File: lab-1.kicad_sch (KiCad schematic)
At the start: 0 parts

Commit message: Added decoupling capacitors
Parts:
- added C0: 4.7u, Capacitor_SMD:C_0201_0603Metric_Pad0.64x0.40mm_HandSolder, symbol Device:C
- added C1, C2, C3, C4, C5: 100n, Capacitor_SMD:C_0201_0603Metric_Pad0.64x0.40mm_HandSolder, symbol Device:C
- added C6: 10n, Capacitor_SMD:C_0201_0603Metric_Pad0.64x0.40mm_HandSolder, symbol Device:C
- added C7, C8: 1u, Capacitor_SMD:C_0201_0603Metric_Pad0.64x0.40mm_HandSolder, symbol Device:C
- added FB1: 120, Inductor_SMD:L_0201_0603Metric_Pad0.64x0.40mm_HandSolder, symbol Device:FerriteBead
- added U1: STM32F405RGTx, Package_QFP:LQFP-64_10x10mm_P0.5mm, symbol MCU_ST_STM32F4:STM32F405RGTx
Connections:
- new net +3.3V: C0.1, C1.1, C2.1, C3.1, C4.1, C5.1, C8.1, FB1.2, U1.1 (VBAT), U1.19 (VDD), U1.32 (VDD), U1.48 (VDD), U1.64 (VDD)
- new net +3.3VA: C6.1, C7.1, FB1.1, U1.13 (VDDA)
- new net GND: C0.2, C1.2, C2.2, C3.2, C4.2, C5.2, C6.2, C7.2, C8.2, U1.12 (VSSA), U1.18 (VSS), U1.63 (VSS)

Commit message: Changed the footprints + track width
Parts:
- C0, C7, C8: footprint Capacitor_SMD:C_0201_0603Metric_Pad0.64x0.40mm_HandSolder -> Capacitor_SMD:C_0603_1608Metric
- C1, C2, C3, C4, C5, C6: footprint Capacitor_SMD:C_0201_0603Metric_Pad0.64x0.40mm_HandSolder -> Capacitor_SMD:C_0402_1005Metric
- FB1: footprint Inductor_SMD:L_0201_0603Metric_Pad0.64x0.40mm_HandSolder -> Inductor_SMD:L_0603_1608Metric
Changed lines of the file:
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@@
 			)
 		)
-		(property "Footprint" "Capacitor_SMD:C_0201_0603Metric_Pad0.64x0.40mm_HandSolder"
+		(property "Footprint" "Capacitor_SMD:C_0402_1005Metric"
 			(at 176.2252 38.1 0)
 			(effects
@@
 			)
 		)
-		(property "Footprint" "Capacitor_SMD:C_0201_0603Metric_Pad0.64x0.40mm_HandSolder"
+		(property "Footprint" "Capacitor_SMD:C_0402_1005Metric"
 			(at 134.3152 38.1 0)
 			(effects
@@
 			)
 		)
-		(property "Footprint" "Capacitor_SMD:C_0201_0603Metric_Pad0.64x0.40mm_HandSolder"
+		(property "Footprint" "Capacitor_SMD:C_0603_1608Metric"
 			(at 210.5152 38.1 0)
 			(effects
@@
 			)
 		)
-		(property "Footprint" "Capacitor_SMD:C_0201_0603Metric_Pad0.64x0.40mm_HandSolder"
+		(property "Footprint" "Capacitor_SMD:C_0402_1005Metric"
 			(at 113.9952 38.1 0)
 			(effects
@@
 			)
 		)
-		(property "Footprint" "Capacitor_SMD:C_0201_0603Metric_Pad0.64x0.40mm_HandSolder"
+		(property "Footprint" "Capacitor_SMD:C_0402_1005Metric"
 			(at 124.1552 38.1 0)
 			(effects
@@
 			)
 		)
-		(property "Footprint" "Capacitor_SMD:C_0201_0603Metric_Pad0.64x0.40mm_HandSolder"
+		(property "Footprint" "Capacitor_SMD:C_0402_1005Metric"
 			(at 93.6752 38.1 0)
 			(effects
@@
 			)
 		)
-		(property "Footprint" "Capacitor_SMD:C_0201_0603Metric_Pad0.64x0.40mm_HandSolder"
+		(property "Footprint" "Capacitor_SMD:C_0402_1005Metric"
 			(at 103.8352 38.1 0)
 			(effects
@@
 			)
 		)
-		(property "Footprint" "Capacitor_SMD:C_0201_0603Metric_Pad0.64x0.40mm_HandSolder"
+		(property "Footprint" "Capacitor_SMD:C_0603_1608Metric"
 			(at 186.3852 38.1 0)
 			(effects
@@
 			)
 		)
-		(property "Footprint" "Inductor_SMD:L_0201_0603Metric_Pad0.64x0.40mm_HandSolder"
+		(property "Footprint" "Inductor_SMD:L_0603_1608Metric"
 			(at 198.12 30.988 90)
 			(effects
@@
 			)
 		)
-		(property "Footprint" "Capacitor_SMD:C_0201_0603Metric_Pad0.64x0.40mm_HandSolder"
+		(property "Footprint" "Capacitor_SMD:C_0603_1608Metric"
 			(at 83.5152 38.1 0)
 			(effects

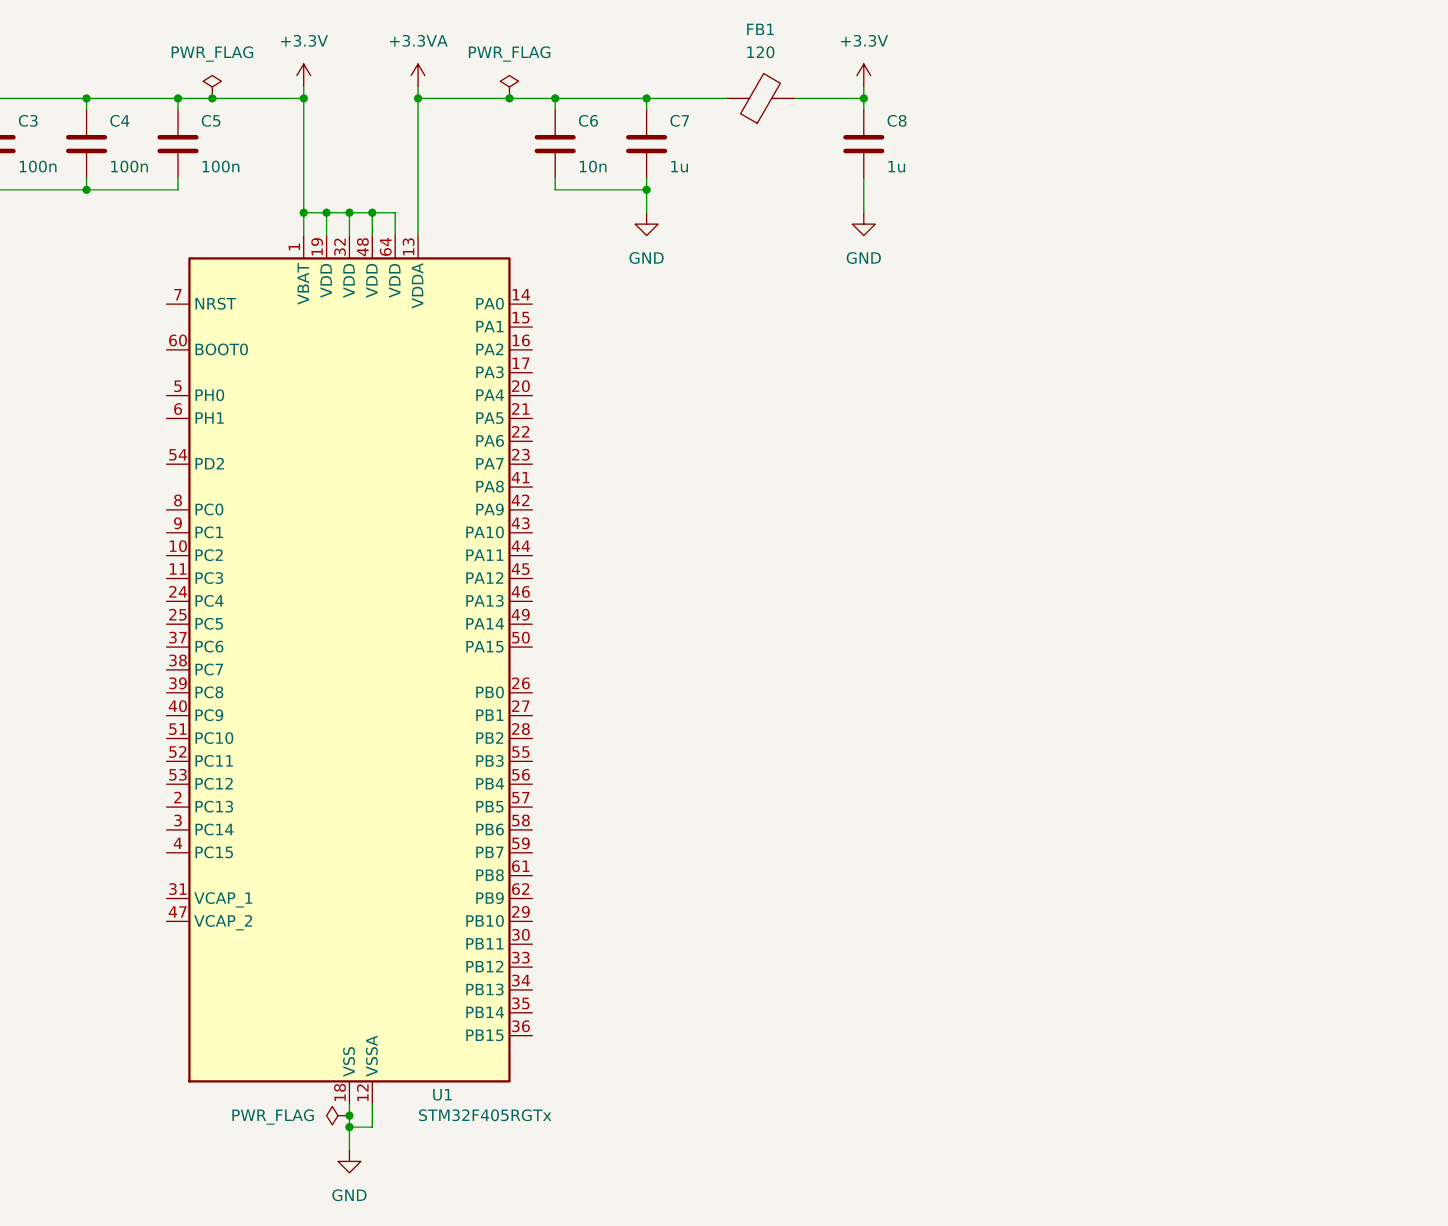
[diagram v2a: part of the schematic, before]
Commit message: Modified tracks and capacitor placing Added type-c and LDO MCP1700 as source of power for STM
Signed-off-by: Yehor Bilous <bilous801@gmail.com>
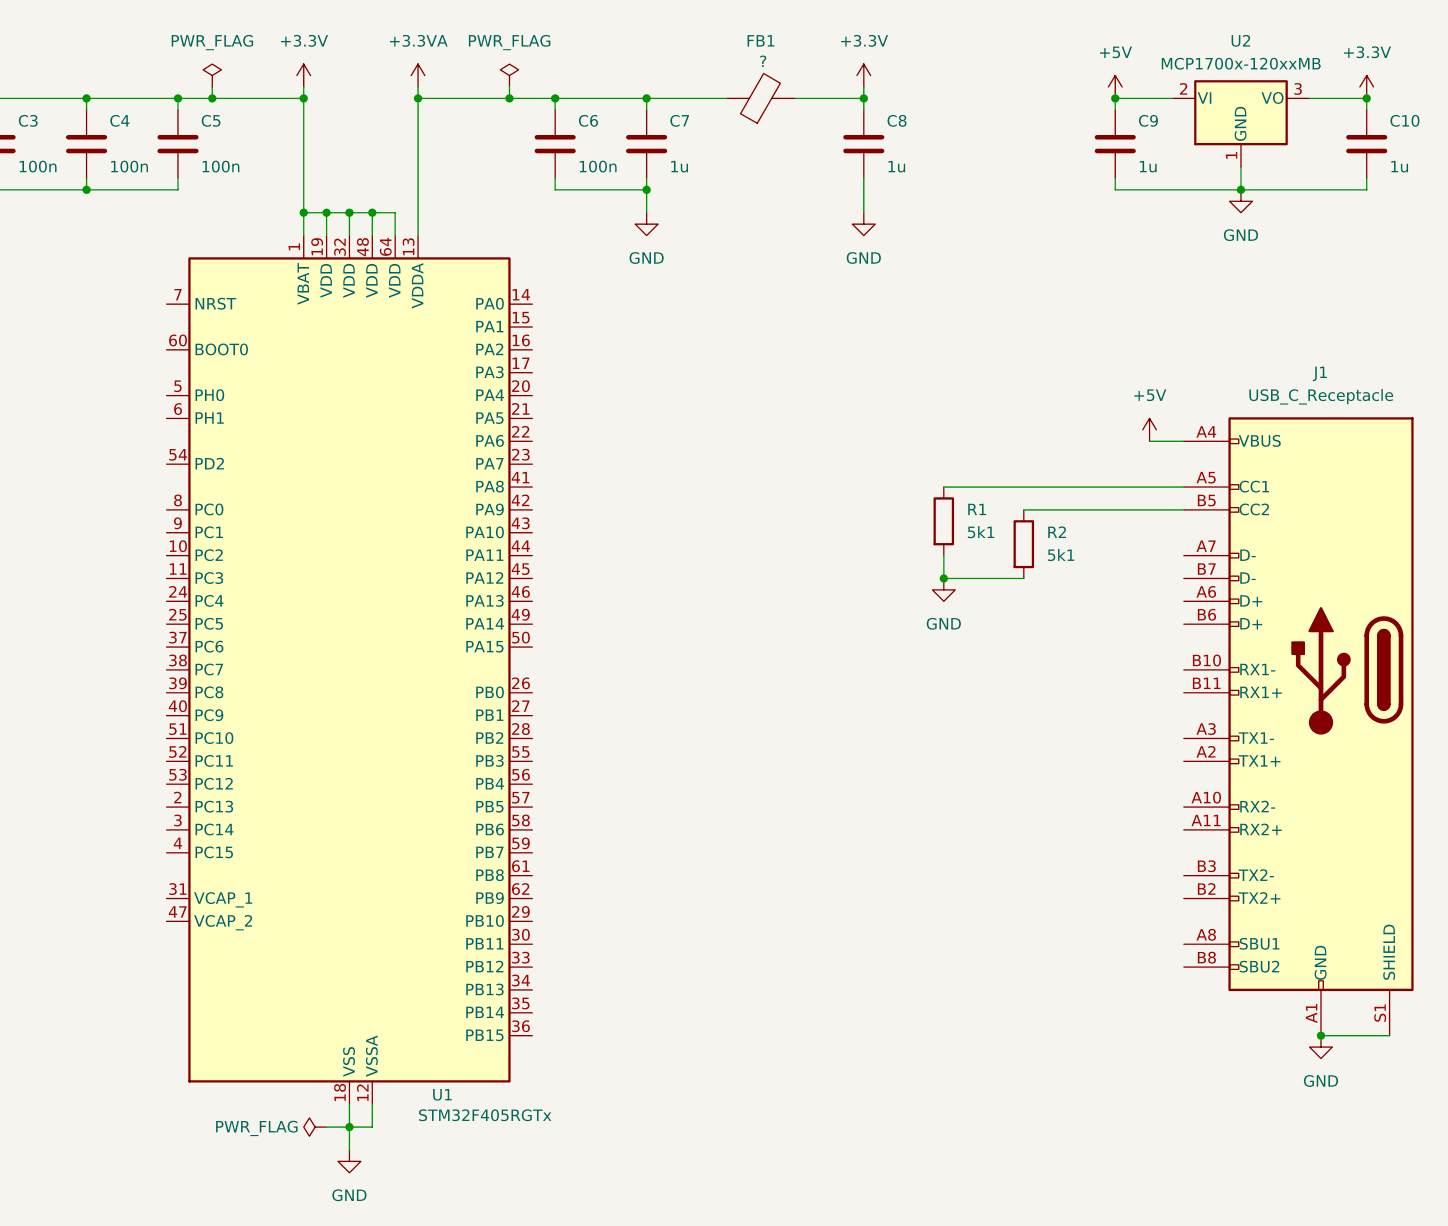
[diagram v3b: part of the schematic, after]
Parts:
- added C10, C9: 1u, Capacitor_SMD:C_0603_1608Metric, symbol Device:C
- added J1: USB_C_Receptacle, Connector_USB:USB_C_Receptacle_Amphenol_12401610E4-2A, symbol Connector:USB_C_Receptacle
- added R1, R2: 5k1, Resistor_SMD:R_0603_1608Metric, symbol Device:R
- added U2: MCP1700x-120xxMB, Package_TO_SOT_SMD:SOT-89-3, symbol Regulator_Linear:MCP1700x-120xxMB
- C6: value 10n -> 100n
- FB1: value 120 -> ?
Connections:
- net +3.3V: now also C10.1, U2.3 (VO)
- net GND: now also C10.2, C9.2, J1.A1 (GND), J1.A12 (GND), J1.B1 (GND), J1.B12 (GND), J1.S1 (SHIELD), R1.2, R2.2, U2.1 (GND)
- new net: J1.A5 (CC1), R1.1
- new net: J1.B5 (CC2), R2.1
- new net +5V: C9.1, J1.A4 (VBUS), J1.A9 (VBUS), J1.B4 (VBUS), J1.B9 (VBUS), U2.2 (VI)

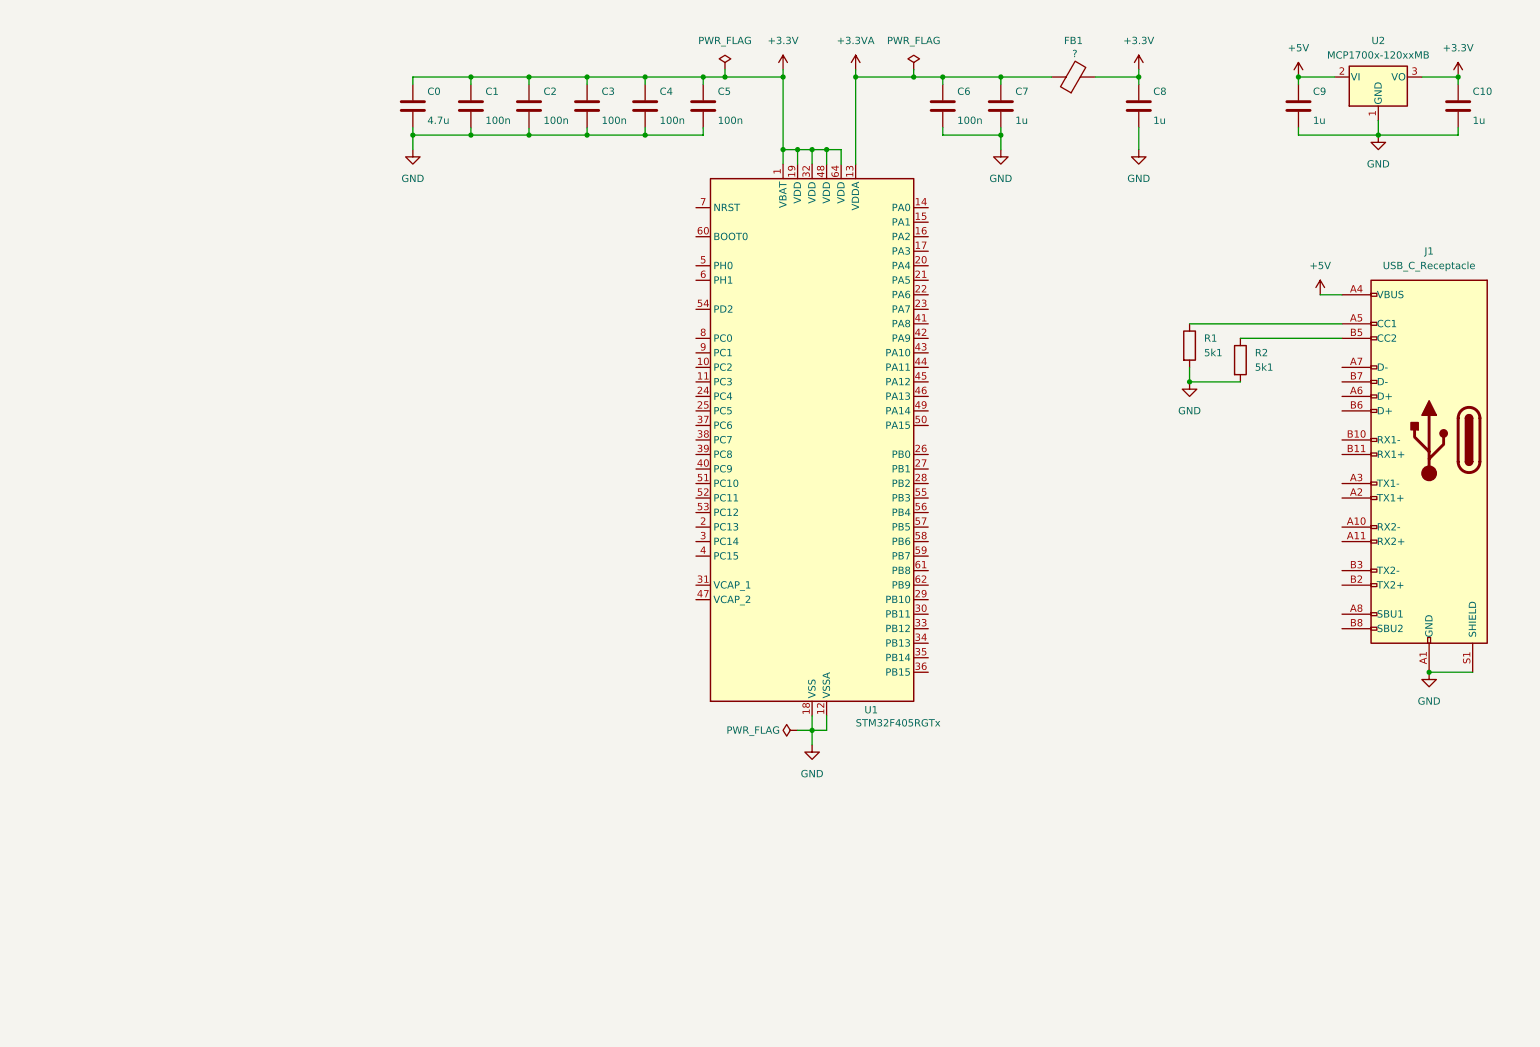
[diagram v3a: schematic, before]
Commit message: add a programmer header and power ORing
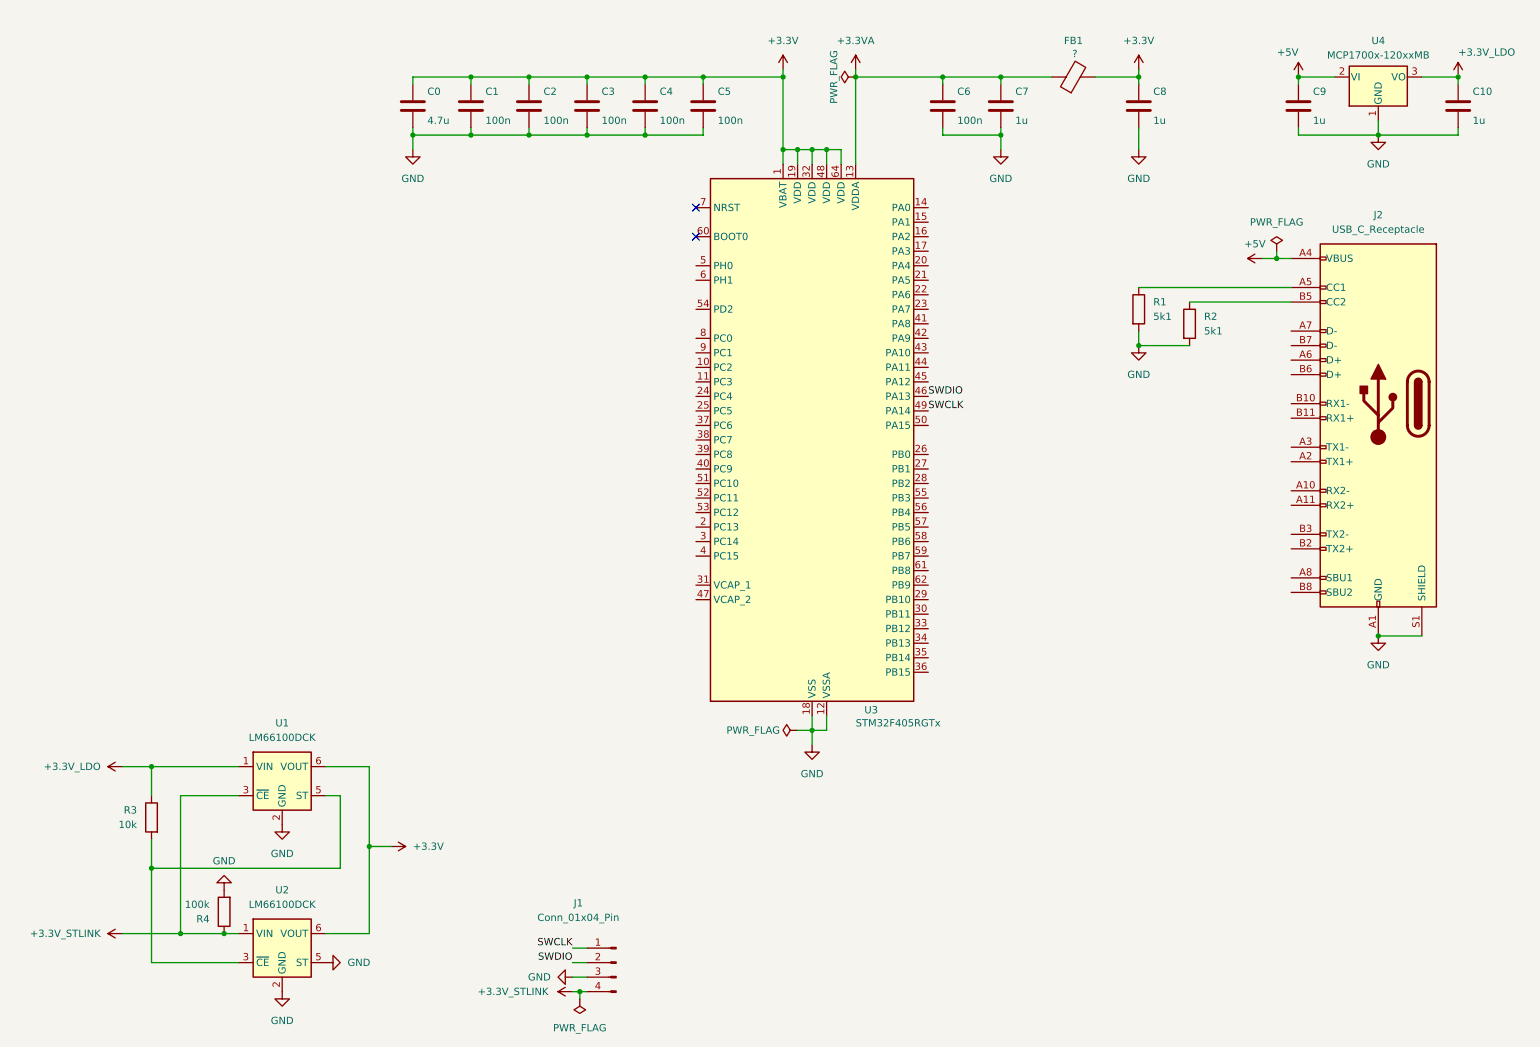
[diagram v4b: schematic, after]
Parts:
- added J1: Conn_01x04_Pin, Connector_PinHeader_2.54mm:PinHeader_1x04_P2.54mm_Vertical, symbol Connector:Conn_01x04_Pin
- added R3: 10k, Resistor_SMD:R_0603_1608Metric, symbol Device:R
- added R4: 100k, Resistor_SMD:R_0603_1608Metric, symbol Device:R
- added U1, U2: LM66100DCK, Package_TO_SOT_SMD:SOT-363_SC-70-6, symbol Power_Management:LM66100DCK
- renumbered J1 to J2, U1 to U3, U2 to U4
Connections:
- net +3.3V: now also U1.6 (VOUT), U2.6 (VOUT); no longer C10.1, U4.3 (VO)
- net GND: now also J1.3 (Pin_3), R4.2, U1.2 (GND), U2.2 (GND), U2.5 (ST)
- net SWDIO: now reaches U3.46 (PA13)
- net SWDIO: now also J1.2 (Pin_2)
- net SWCLK: now reaches U3.49 (PA14)
- net SWCLK: now also J1.1 (Pin_1)
- new net: R3.2, U1.5 (ST), U2.3 (~{CE})
- new net +3.3V_LDO: C10.1, R3.1, U1.1 (VIN), U4.3 (VO)
- new net +3.3V_STLINK: J1.4 (Pin_4), R4.1, U1.3 (~{CE}), U2.1 (VIN)
- no-connect marks 0 -> 2
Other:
- moved on the sheet: J2, R1, R2

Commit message: add crystal
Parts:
- added C11, C12: 22pF, Capacitor_SMD:C_0402_1005Metric, symbol Device:C
- added Y1: 8 MHz, Crystal:Crystal_SMD_2520-4Pin_2.5x2.0mm, symbol Device:Crystal
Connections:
- net GND: now also C11.1, C12.1
- net OSC_IN: now reaches U3.5 (PH0)
- net OSC_IN: now also C11.2, Y1.2
- net OSC_OUT: now reaches U3.6 (PH1)
- net OSC_OUT: now also C12.2, Y1.1
